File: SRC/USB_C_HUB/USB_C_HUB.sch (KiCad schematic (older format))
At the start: 45 parts, among them J1 USB_C_Receptacle, J10 USB_C_Receptacle_USB2.0, J2 USB3_A, J3 USB3_A, J4 USB_C_Receptacle, P1 USB_C_Plug, U1 HD3SS460, U2 SY6280, U3 SY6280, U4 SY6280, U5 SY6280

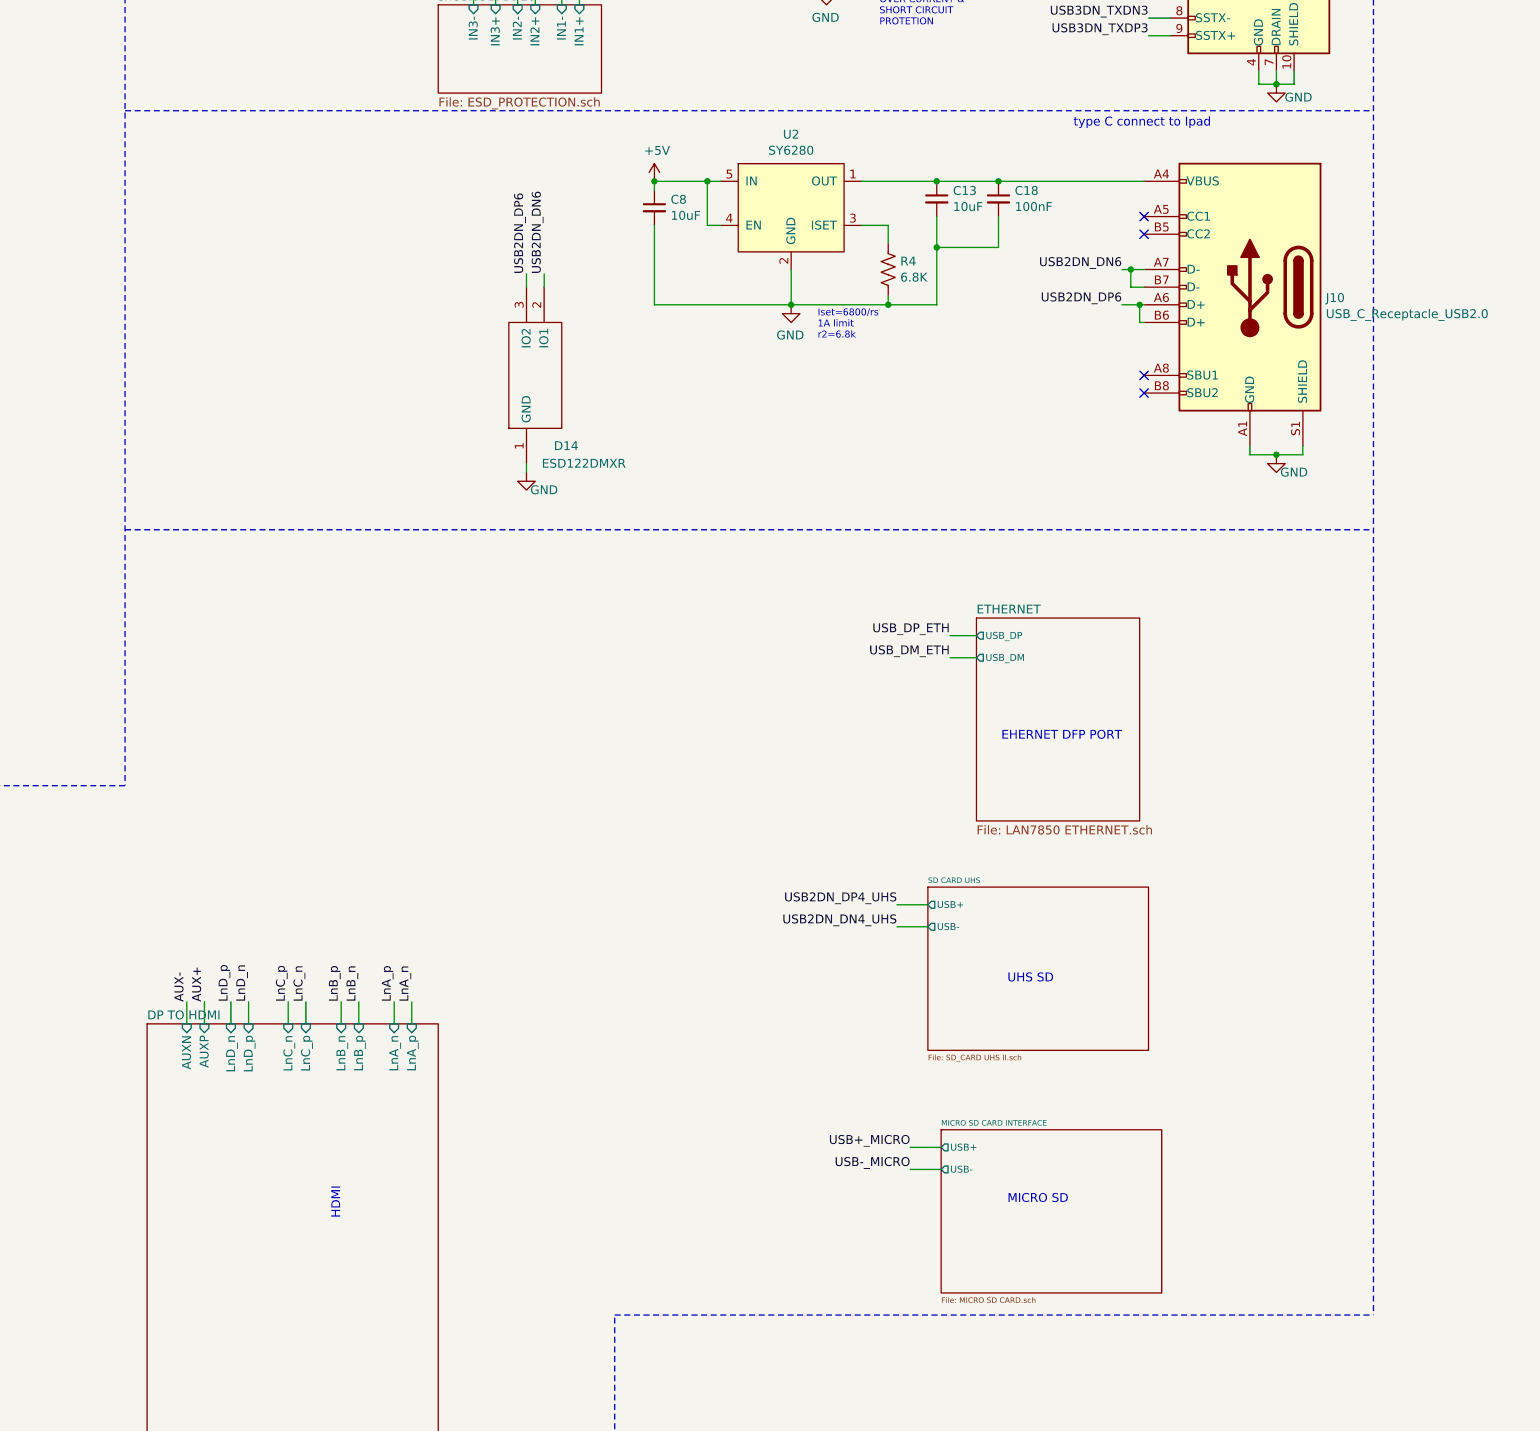
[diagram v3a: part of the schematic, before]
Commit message: updated BOM, minor change in schematic
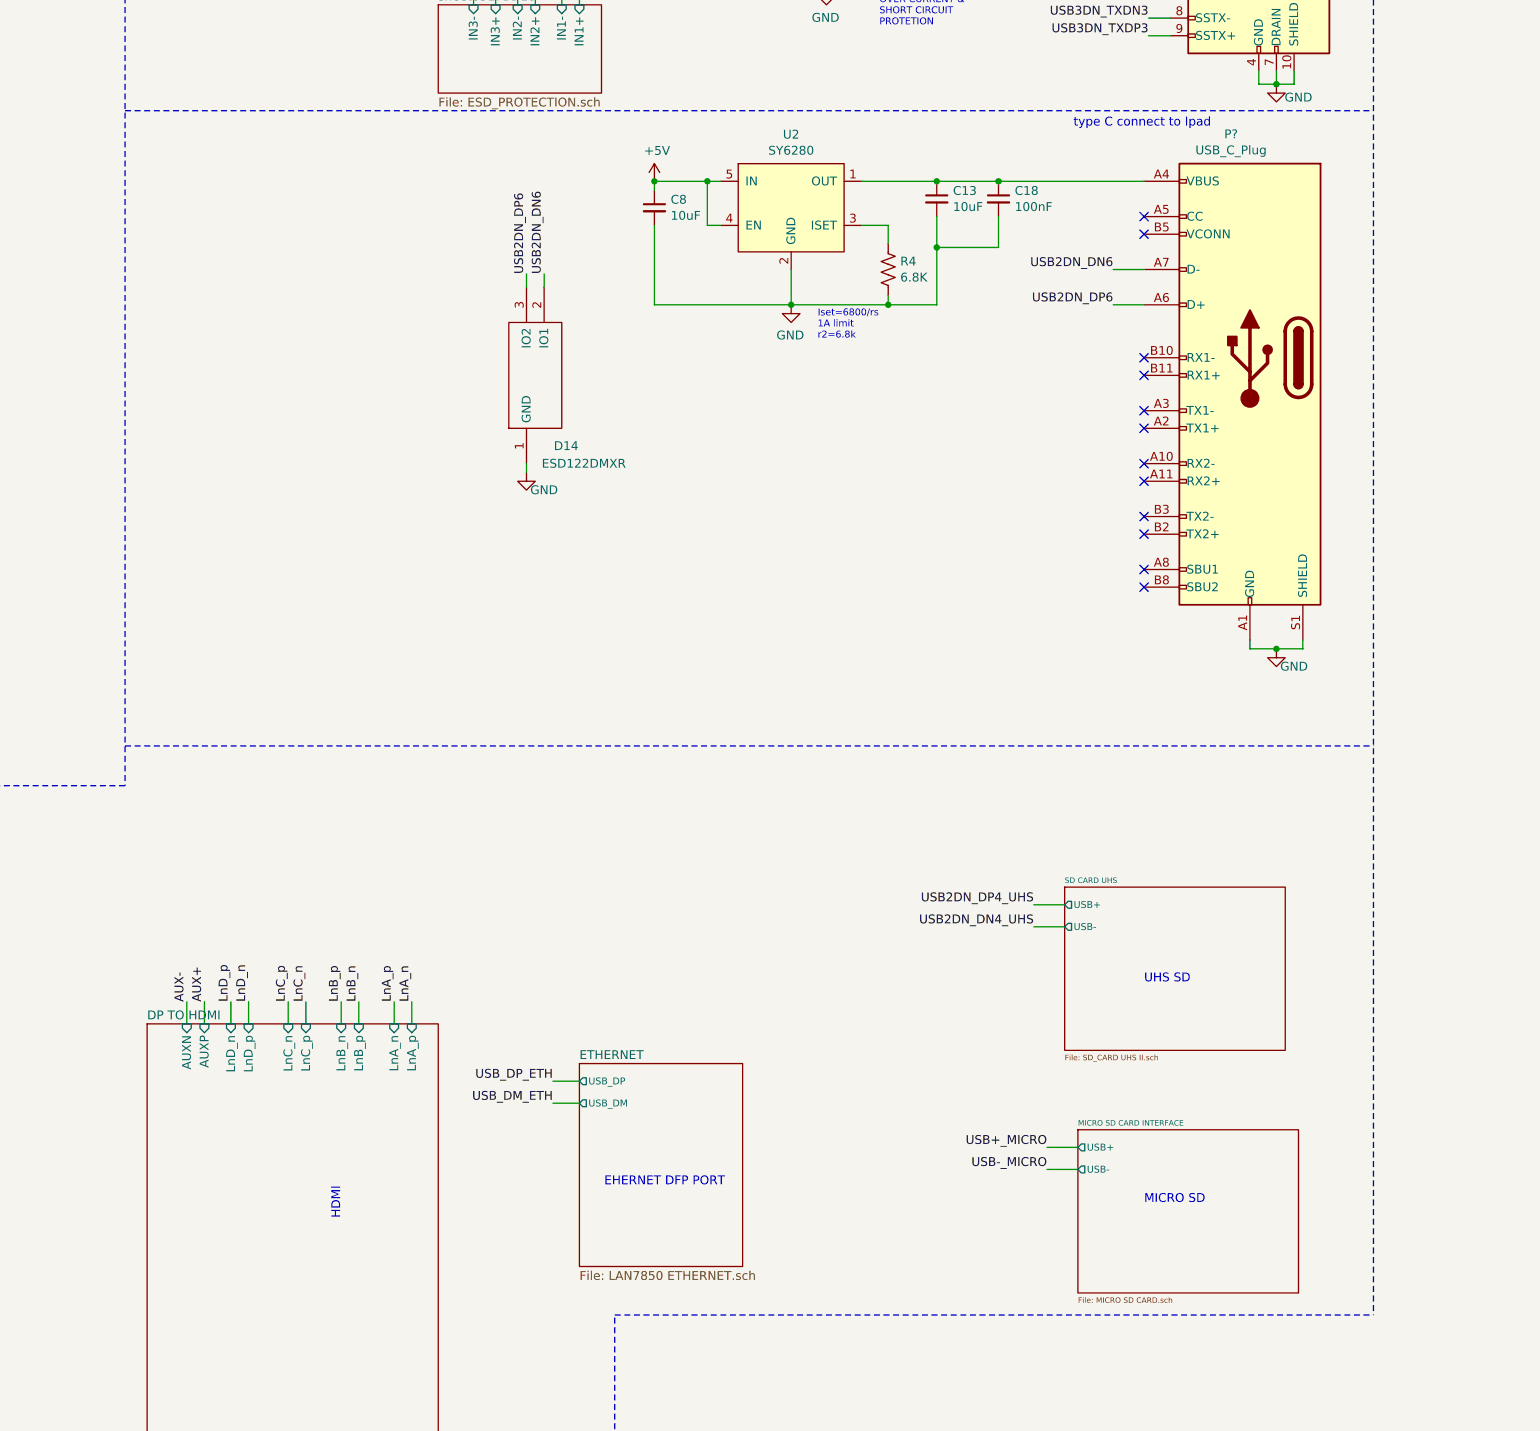
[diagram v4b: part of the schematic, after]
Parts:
- removed J10: USB_C_Receptacle_USB2.0, footprints:GCT_USB4105_REVA, symbol Connector:USB_C_Receptacle_USB2.0
- added P?: USB_C_Plug, footprints:USB_C_PLUG_GCT_USB4155-03-C_REVA, symbol Connector:USB_C_Plug
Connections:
- net GND: now also P?.A1 (GND), P?.A12 (GND), P?.B1 (GND), P?.B12 (GND), P?.S1 (SHIELD)
- net USB2DN_DN6: now also P?.A7 (D-)
- net USB2DN_DP6: now also P?.A6 (D+)
- net at C13.1, C18.1, U2.1 (OUT): now also P?.A4 (VBUS), P?.A9 (VBUS), P?.B4 (VBUS), P?.B9 (VBUS)
- no-connect marks 32 -> 40
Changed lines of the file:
@@
 Text Label 11900 3300 0    50   ~ 0
 USB2DN_DN3
-Text Label 20025 12250 2    50   ~ 0
+Text Label 20800 12250 2    50   ~ 0
 USB2DN_DP4_UHS
-Text Label 20025 12375 2    50   ~ 0
+Text Label 20800 12375 2    50   ~ 0
 USB2DN_DN4_UHS
 Wire Wire Line
-	20200 12375 20025 12375
-Wire Wire Line
-	20025 12250 20200 12250
+	20975 12375 20800 12375
+Wire Wire Line
+	20800 12250 20975 12250
 $Comp
 L usb_hub:SY6280 U3
@@
 NoConn ~ 11900 4225
 Wire Wire Line
-	20275 13750 20100 13750
-Wire Wire Line
-	20100 13625 20275 13625
+	21050 13750 20875 13750
+Wire Wire Line
+	20875 13625 21050 13625
 $Sheet
-S 20275 13525 1250 925
+S 21050 13525 1250 925
 U 66525694
 F0 "MICRO SD CARD INTERFACE" 31
 F1 "MICRO SD CARD.sch" 31
-F2 "USB+" O L 20275 13625 39
-F3 "USB-" O L 20275 13750 39
+F2 "USB+" O L 21050 13625 39
+F3 "USB-" O L 21050 13750 39
 $EndSheet
 Text Label 14175 3975 0    50   ~ 0
@@
 Text Label 14175 4050 0    50   ~ 0
 USB2DN_DN4_UHS
-Text Label 20100 13750 2    50   ~ 0
+Text Label 20875 13750 2    50   ~ 0
 USB-_MICRO
-Text Label 20100 13625 2    50   ~ 0
+Text Label 20875 13625 2    50   ~ 0
 USB+_MICRO
 Text Label 14250 3475 0    50   ~ 0
@@
 F7 "IN3-" I T 17500 5050 50
 $EndSheet
-Connection ~ 22175 9700
-Wire Wire Line
-	22325 9700 22175 9700
-Wire Wire Line
-	22325 9650 22325 9700
-Wire Wire Line
-	22025 9700 22175 9700
-Wire Wire Line
-	22025 9650 22025 9700
+Connection ~ 22175 10800
+Wire Wire Line
+	22325 10800 22175 10800
+Wire Wire Line
+	22325 10750 22325 10800
+Wire Wire Line
+	22025 10800 22175 10800
+Wire Wire Line
+	22025 10750 22025 10800
 $Comp
 L OLIMEX_Power:GND #PWR?
 U 1 1 6247988A
-P 22175 9700
+P 22175 10800
 AR Path="/619540C6/6247988A" Ref="#PWR?"  Part="1"
 AR Path="/6247988A" Ref="#PWR018"  Part="1"
-F 0 "#PWR018" H 22175 9450 50  0001 C CNN
-F 1 "GND" H 22075 9600 50  0000 C CNN
-F 2 "" H 22175 9700 60  0000 C CNN
-F 3 "" H 22175 9700 60  0000 C CNN
-	1    22175 9700
+F 0 "#PWR018" H 22175 10550 50  0001 C CNN
+F 1 "GND" H 22075 10700 50  0000 C CNN
+F 2 "" H 22175 10800 60  0000 C CNN
+F 3 "" H 22175 10800 60  0000 C CNN
+	1    22175 10800
 	-1   0    0    -1
 $EndComp
-Text Label 21300 8850 2    50   ~ 0
-USB2DN_DP6
-Text Label 21300 8650 2    50   ~ 0
-USB2DN_DN6
-Wire Wire Line
-	21425 8650 21350 8650
-NoConn ~ 21425 8450
-NoConn ~ 21425 8350
 Wire Wire Line
 	20250 8150 20600 8150
@@
 Text Notes 17300 5650 0    39   ~ 0
 ESD PROTECTION
-Wire Wire Line
-	20475 10725 20325 10725
-Wire Wire Line
-	20475 10850 20325 10850
-Text Notes 21300 11325 2    50   ~ 0
-EHERNET DFP PORT
-$Sheet
-S 20475 10625 925  1150
-U 631C6BCF
-F0 "ETHERNET" 50
-F1 "LAN7850 ETHERNET.sch" 50
-F2 "USB_DP" O L 20475 10725 39
-F3 "USB_DM" O L 20475 10850 39
-$EndSheet
-Text Label 20325 10725 2    50   ~ 0
-USB_DP_ETH
-Text Label 20325 10850 2    50   ~ 0
-USB_DM_ETH
 Text Notes 13900 14025 3    50   ~ 0
 SATA\n
-Text Notes 20650 13950 0    50   ~ 0
+Text Notes 21425 13950 0    50   ~ 0
 MICRO SD
 Text Notes 16875 13850 3    50   ~ 0
 HDMI
-Text Notes 20650 12700 0    50   ~ 0
+Text Notes 21425 12700 0    50   ~ 0
 UHS SD
 $Sheet
-S 20200 12150 1250 925
+S 20975 12150 1250 925
 U 63D2BAD4
 F0 "SD CARD UHS" 31
 F1 "SD_CARD UHS II.sch" 31
-F2 "USB+" O L 20200 12250 39
-F3 "USB-" O L 20200 12375 39
+F2 "USB+" O L 20975 12250 39
+F3 "USB-" O L 20975 12375 39
 $EndSheet
 Text Notes 2000 6725 0    98   ~ 20
@@
 	22725 700  22725 14575
 Wire Notes Line
-	15650 10125 22725 10125
+	15650 11350 22725 11350
 Wire Notes Line
 	15650 7750 22725 7750
@@
 HEADPHONE JACK\n
 $Comp
-L Connector:USB_C_Receptacle_USB2.0 J10
-U 1 1 650E46E9
-P 22025 8750
-F 0 "J10" H 21595 8689 50  0000 R CNN
-F 1 "USB_C_Receptacle_USB2.0" H 21595 8598 50  0000 R CNN
-F 2 "footprints:GCT_USB4105_REVA" H 22175 8750 50  0001 C CNN
-F 3 "https://www.usb.org/sites/default/files/documents/usb_type-c.zip" H 22175 8750 50  0001 C CNN
-	1    22025 8750
-	-1   0    0    -1
-$EndComp
-NoConn ~ 21425 9250
-NoConn ~ 21425 9350
-$Comp
 L OLIMEX_Power:GND #PWR?
 U 1 1 617FB915
@@
 	-1   0    0    -1
 $EndComp
-Wire Wire Line
-	21425 8750 21350 8750
-Wire Wire Line
-	21350 8750 21350 8650
-Connection ~ 21350 8650
-Wire Wire Line
-	21350 8650 21300 8650
-Wire Wire Line
-	21400 8850 21400 8950
-Wire Wire Line
-	21400 8950 21425 8950
-Wire Wire Line
-	21300 8850 21400 8850
-Connection ~ 21400 8850
-Wire Wire Line
-	21400 8850 21425 8850
+NoConn ~ 21425 8350
+NoConn ~ 21425 8450
+Text Label 21250 8850 2    50   ~ 0
+USB2DN_DP6
+Text Label 21250 8650 2    50   ~ 0
+USB2DN_DN6
+Wire Wire Line
+	21425 8650 21250 8650
+Wire Wire Line
+	21250 8850 21425 8850
+NoConn ~ 21425 9150
+NoConn ~ 21425 9250
+NoConn ~ 21425 9450
+NoConn ~ 21425 9550
+NoConn ~ 21425 9750
+NoConn ~ 21425 9850
+NoConn ~ 21425 10050
+NoConn ~ 21425 10150
+NoConn ~ 21425 10350
+NoConn ~ 21425 10450
+$Comp
+L Connector:USB_C_Plug P?
+U 1 1 618905E9
+P 22025 9150
+F 0 "P?" H 22132 10417 50  0000 C CNN
+F 1 "USB_C_Plug" H 22132 10326 50  0000 C CNN
+F 2 "footprints:USB_C_PLUG_GCT_USB4155-03-C_REVA" H 22175 9150 50  0001 C CNN
+F 3 "https://www.usb.org/sites/default/files/documents/usb_type-c.zip" H 22175 9150 50  0001 C CNN
+	1    22025 9150
+	-1   0    0    -1
+$EndComp
+Text Label 18075 13375 2    50   ~ 0
+USB_DM_ETH
+Text Label 18075 13250 2    50   ~ 0
+USB_DP_ETH
+$Sheet
+S 18225 13150 925  1150
+U 631C6BCF
+F0 "ETHERNET" 50
+F1 "LAN7850 ETHERNET.sch" 50
+F2 "USB_DP" O L 18225 13250 39
+F3 "USB_DM" O L 18225 13375 39
+$EndSheet
+Text Notes 19050 13850 2    50   ~ 0
+EHERNET DFP PORT
+Wire Wire Line
+	18225 13375 18075 13375
+Wire Wire Line
+	18225 13250 18075 13250
 $EndSCHEMATC
